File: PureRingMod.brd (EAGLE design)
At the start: 99 x 69.5 mm, 37 parts, among them IC1 TL074P, IC2 TL072P, X1 NC3FD-V

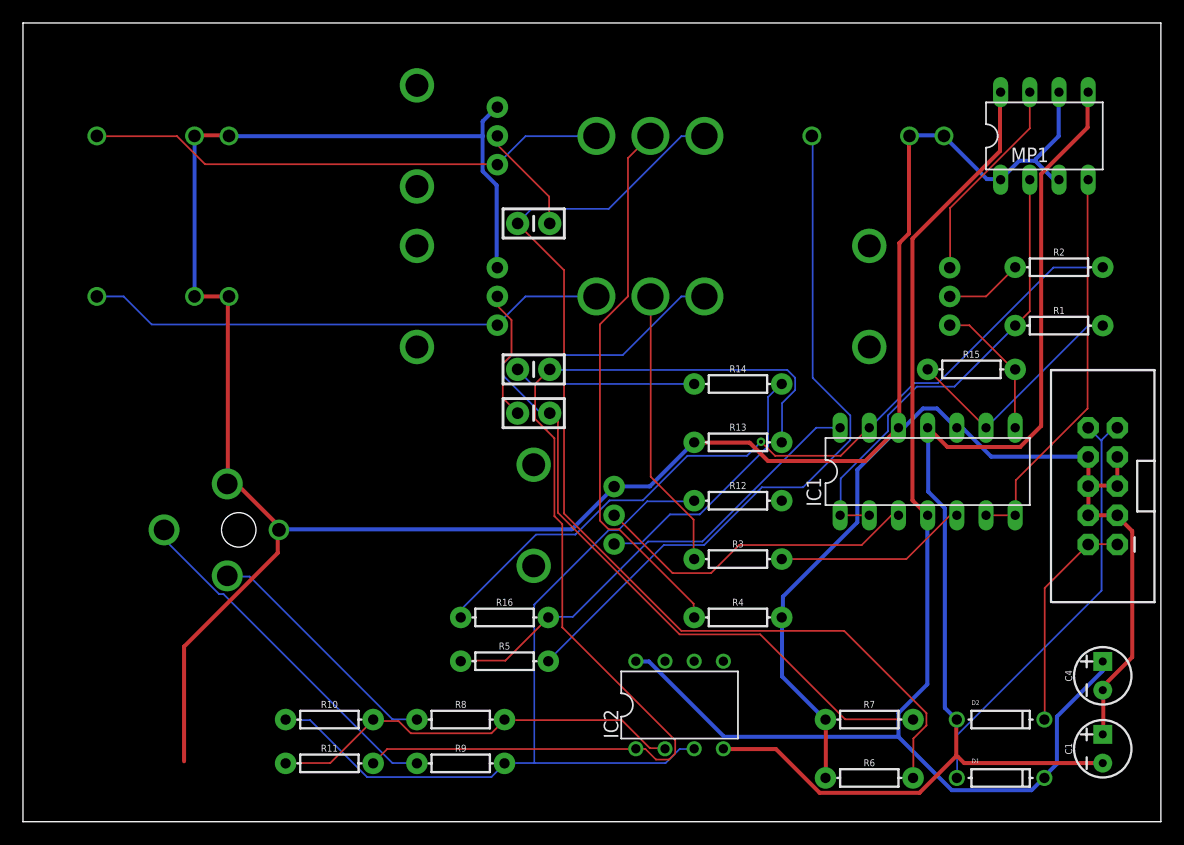
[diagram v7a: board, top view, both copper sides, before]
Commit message: fixed -12V to Tl074
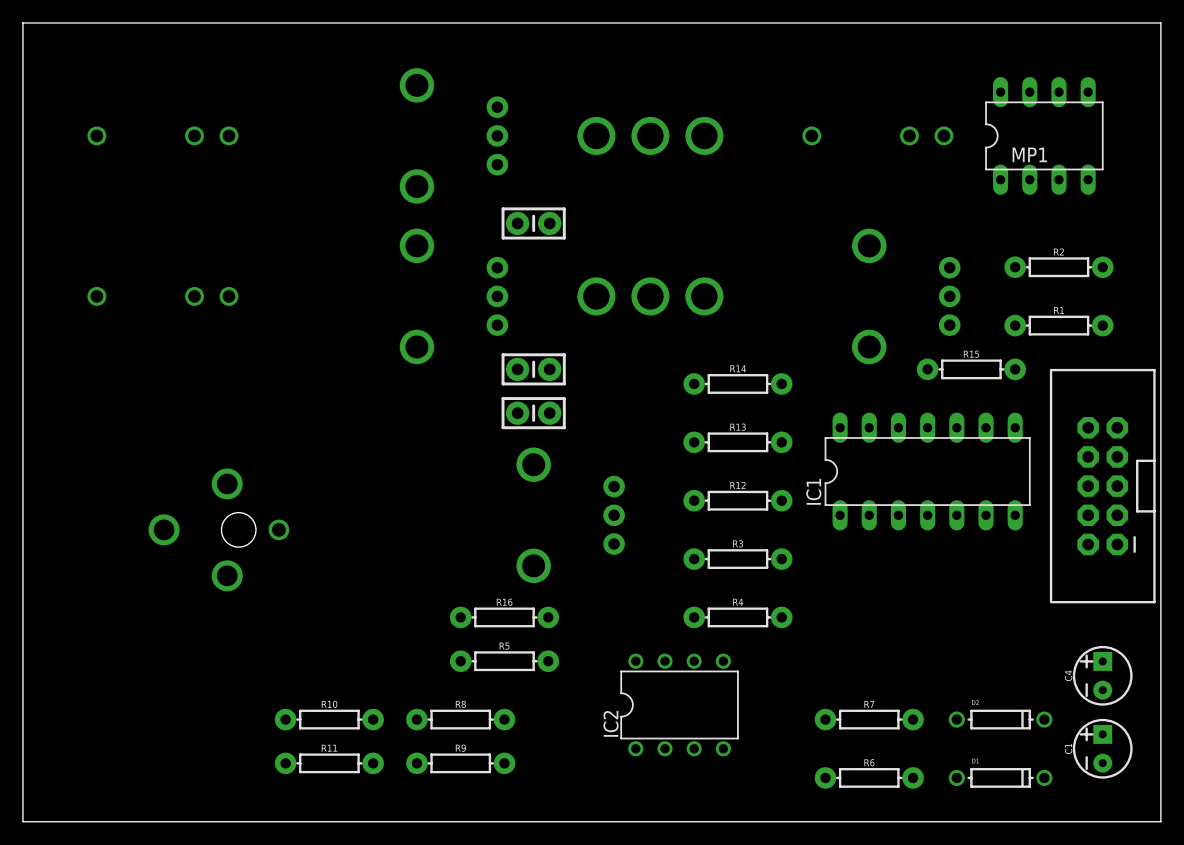
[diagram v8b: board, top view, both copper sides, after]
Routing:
- net GND: track 299.8 -> 0.00 mm
- net +12V: track 113.8 -> 0.00 mm
- net -12V: track 108.0 -> 0.00 mm
- net N$27: track 94.2 -> 0.00 mm
- net N$20: track 91.2 -> 0.00 mm
- net N$21: track 73.7 -> 0.00 mm
- net N$25: track 70.2 -> 0.00 mm
- net N$7: track 69.9 -> 0.00 mm, vias 1 -> 0
- net N$15: track 62.2 -> 0.00 mm
- net N$8: track 47.7 -> 0.00 mm
- net N$17: track 45.6 -> 0.00 mm
- net N$16: track 45.5 -> 0.00 mm
- net N$12: track 41.5 -> 0.00 mm
- net N$1: track 40.5 -> 0.00 mm
- net N$9: track 38.1 -> 0.00 mm
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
